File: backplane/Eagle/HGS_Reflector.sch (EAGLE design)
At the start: 0 parts

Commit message: handheld ground station eagle mockup
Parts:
- added J1: U.FL, SparkFun-Connectors:U.FL
- added U1: TQP3M9037, U-Qorvo-TQP3M9037-LNA:TQP3M9037
- added X1: MINI-USB-32005-201, con-cypressindustries:MINI-USB-32005-201
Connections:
- new net GND: J1.GND@0, J1.GND@1, J1.SIGNAL, U1.GND

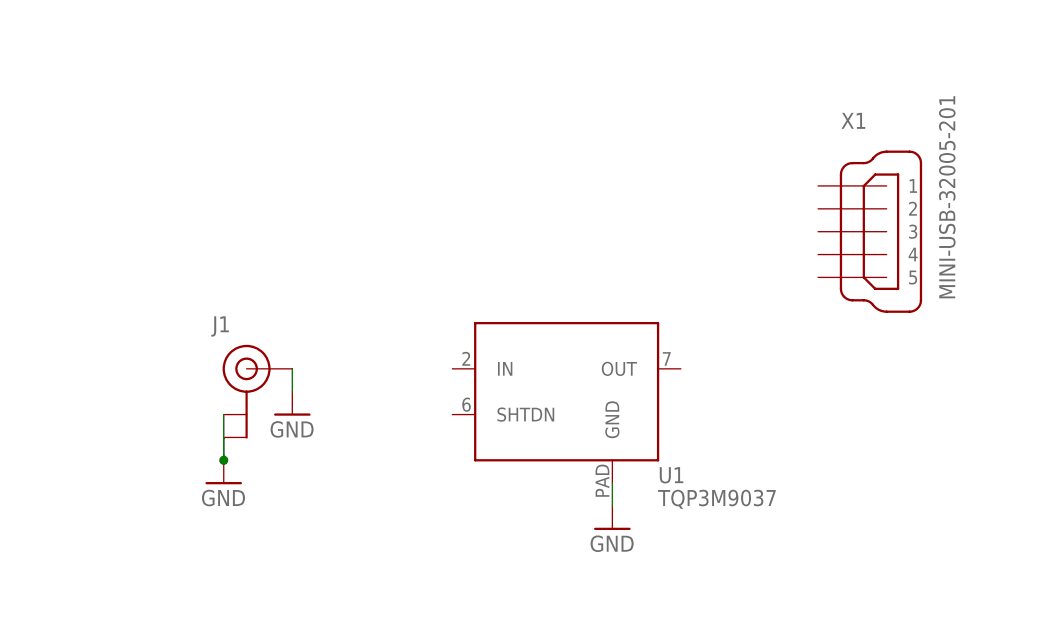
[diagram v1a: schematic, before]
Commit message: updated hgs mockup
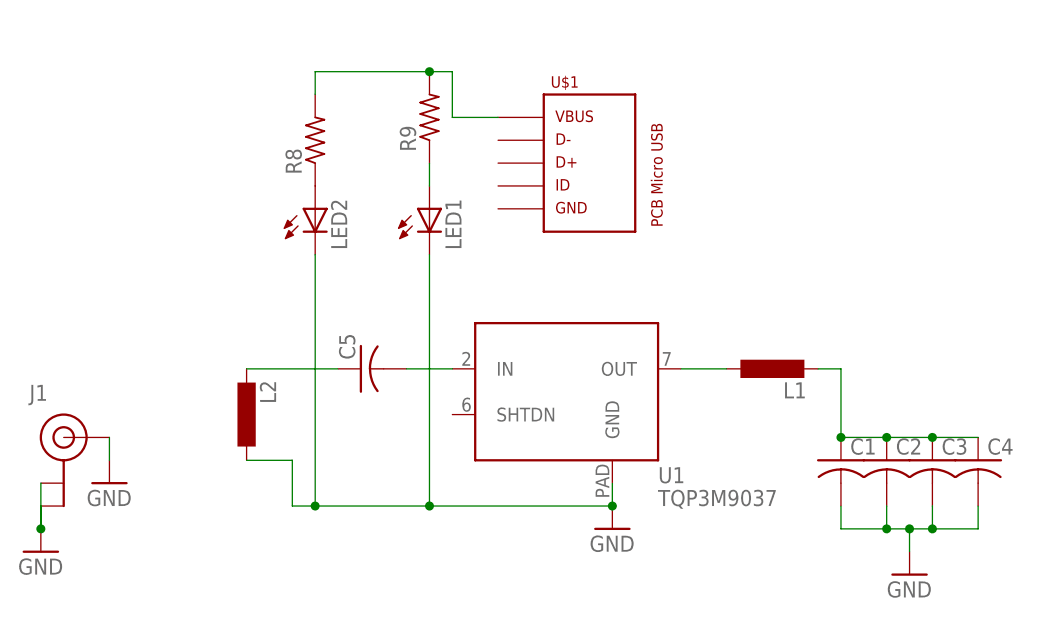
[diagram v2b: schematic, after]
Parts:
- removed X1: MINI-USB-32005-201, con-cypressindustries:MINI-USB-32005-201
- added C1, C2, C3, C4, C5: (no value), rcl:C-USC1210
- added L1, L2: (no value), rcl:L-EUL3216C
- added LED1, LED2: (no value), eagle-ltspice:LED_E
- added R8, R9: (no value), rcl:R-US_R0402
- added U$1: PCB_MICRO_USB_BSS_1, USB_pcb_connectors:PCB_MICRO_USB_BSS_1
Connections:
- new net N$10: LED1.A, R9.1
- new net N$11: R8.2, R9.2, U$1.1
- new net N$5: L1.1, U1.OUT
- new net N$6: C1.1, C2.1, C3.1, C4.1, L1.2
- new net N$7: C5.1, L2.2
- new net N$8: C5.2, U1.IN
- new net N$9: LED2.A, R8.1
- net GND: now also C1.2, C2.2, C3.2, C4.2, L2.1, LED1.C, LED2.C
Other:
- moved on the sheet: J1
